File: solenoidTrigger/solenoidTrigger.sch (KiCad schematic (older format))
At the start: 41 parts, among them J8 CONN_02X03, P1 OSTTC03, P2 OSTTC02, P3 OSTTC08, P4 OSTTC03, P5 OSTTC03, Q1 NMOS_CDS16, Q2 NMOS_CDS16, Q3 NMOS_CDS16, Q4 NMOS_CDS16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

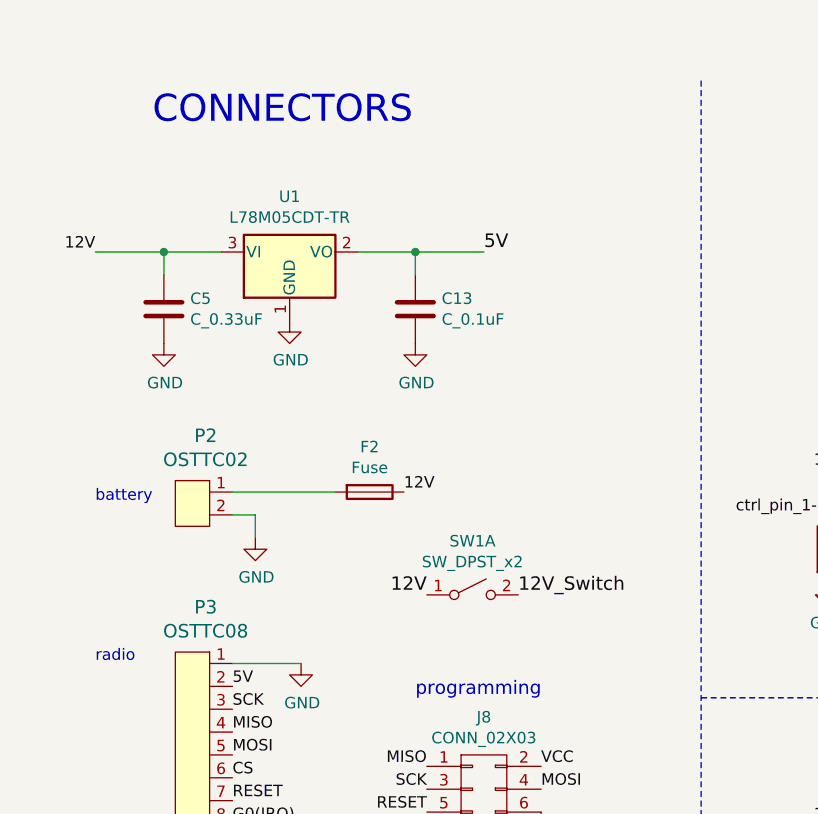
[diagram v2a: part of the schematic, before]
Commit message: Created part for fuse reciprocal, deleted most traces, laying out board again to improve organization and performance
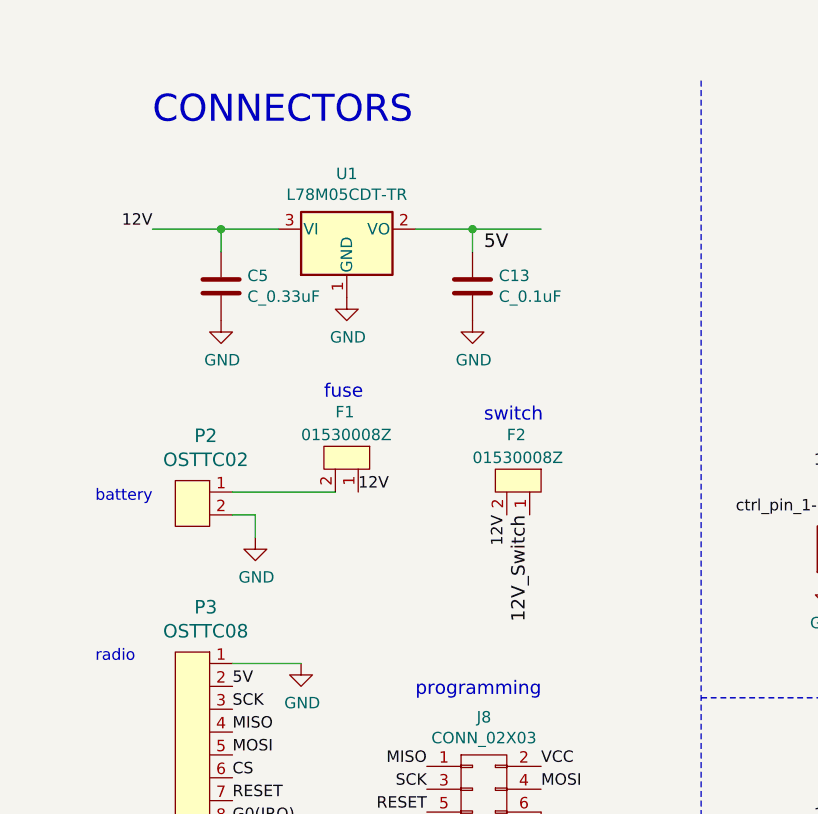
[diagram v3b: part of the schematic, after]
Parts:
- removed F2: Fuse, symbol Device:Fuse
- removed SW1: SW_DPST_x2, symbol Switch:SW_DPST_x2
- added F1, F2: 01530008Z, footprints:01530008Z, symbol Rocketry:01530008Z
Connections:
- net 12V: now also F1.1, F2.2
- net 12V_Switch: now also F2.1
- net VCC: no longer C13.1, U1.2 (VO)
- net at P2.1: now also F1.2
- new net: C13.1, U1.2 (VO)
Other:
- note added: "fuse"
- note added: "switch\n"
- moved on the sheet: C13, C5, U1
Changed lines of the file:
@@
 Text Label 2750 9750 0    50   ~ 0
 12V_Solenoid3
-Text Label 2300 7350 0    50   ~ 0
-12V
 Text Notes 950  7400 0    50   ~ 0
 battery
@@
 Wire Wire Line
 	1650 7450 1650 7550
-$Comp
-L Device:Fuse F2
-U 1 1 5DA01504
-P 2150 7350
-F 0 "F2" V 1953 7350 50  0000 C CNN
-F 1 "Fuse" V 2044 7350 50  0000 C CNN
-F 2 "" V 2080 7350 50  0001 C CNN
-F 3 "~" H 2150 7350 50  0001 C CNN
-	1    2150 7350
-	0    1    1    0
-$EndComp
 Text Notes 2350 8250 0    59   ~ 0
 programming
@@
 L power:GND #PWR0131
 U 1 1 5DDAC02E
-P 2350 6700
-F 0 "#PWR0131" H 2350 6450 50  0001 C CNN
-F 1 "GND" H 2355 6527 50  0000 C CNN
-F 2 "" H 2350 6700 50  0001 C CNN
-F 3 "" H 2350 6700 50  0001 C CNN
-	1    2350 6700
+P 2600 6600
+F 0 "#PWR0131" H 2600 6350 50  0001 C CNN
+F 1 "GND" H 2605 6427 50  0000 C CNN
+F 2 "" H 2600 6600 50  0001 C CNN
+F 3 "" H 2600 6600 50  0001 C CNN
+	1    2600 6600
 	1    0    0    -1
 $EndComp
@@
 L Rocketry:C_0.1uF C13
 U 1 1 5DDAB0AE
-P 2350 6550
-F 0 "C13" H 2465 6596 50  0000 L CNN
-F 1 "C_0.1uF" H 2465 6505 50  0000 L CNN
-F 2 "footprints:C_0805_OEM" H 2388 6400 50  0001 C CNN
-F 3 "http://datasheets.avx.com/X7RDielectric.pdf" H 2375 6650 50  0001 C CNN
-F 4 "DK" H 2350 6550 60  0001 C CNN "MFN"
-F 5 "478-3352-1-ND" H 2350 6550 60  0001 C CNN "MPN"
-F 6 "https://www.digikey.com/products/en?keywords=478-3352-1-ND" H 2775 7050 60  0001 C CNN "PurchasingLink"
-	1    2350 6550
+P 2600 6450
+F 0 "C13" H 2715 6496 50  0000 L CNN
+F 1 "C_0.1uF" H 2715 6405 50  0000 L CNN
+F 2 "footprints:C_0805_OEM" H 2638 6300 50  0001 C CNN
+F 3 "http://datasheets.avx.com/X7RDielectric.pdf" H 2625 6550 50  0001 C CNN
+F 4 "DK" H 2600 6450 60  0001 C CNN "MFN"
+F 5 "478-3352-1-ND" H 2600 6450 60  0001 C CNN "MPN"
+F 6 "https://www.digikey.com/products/en?keywords=478-3352-1-ND" H 3025 6950 60  0001 C CNN "PurchasingLink"
+	1    2600 6450
 	1    0    0    -1
 $EndComp
 Wire Wire Line
-	2350 6300 2650 6300
-Connection ~ 2350 6300
+	2600 6200 2900 6200
+Connection ~ 2600 6200
 Wire Wire Line
-	2350 6300 2350 6400
+	2600 6200 2600 6300
 Wire Wire Line
-	2100 6300 2350 6300
+	2350 6200 2600 6200
 Text Label 2650 6300 0    59   ~ 0
 5V
@@
 L power:GND #PWR0124
 U 1 1 5DD00003
-P 1250 6700
-F 0 "#PWR0124" H 1250 6450 50  0001 C CNN
-F 1 "GND" H 1255 6527 50  0000 C CNN
-F 2 "" H 1250 6700 50  0001 C CNN
-F 3 "" H 1250 6700 50  0001 C CNN
-	1    1250 6700
+P 1500 6600
+F 0 "#PWR0124" H 1500 6350 50  0001 C CNN
+F 1 "GND" H 1505 6427 50  0000 C CNN
+F 2 "" H 1500 6600 50  0001 C CNN
+F 3 "" H 1500 6600 50  0001 C CNN
+	1    1500 6600
 	1    0    0    -1
 $EndComp
 Wire Wire Line
-	1250 6300 1500 6300
-Connection ~ 1250 6300
+	1500 6200 1750 6200
+Connection ~ 1500 6200
 Wire Wire Line
-	1250 6300 1250 6400
+	1500 6200 1500 6300
 Wire Wire Line
-	950  6300 1250 6300
+	1200 6200 1500 6200
 $Comp
 L Rocketry:C_0.33uF C5
 U 1 1 5DEDBC87
-P 1250 6550
-F 0 "C5" H 1135 6504 50  0000 R CNN
-F 1 "C_0.33uF" H 1135 6595 50  0000 R CNN
-F 2 "footprints:C_0805_OEM" H 1288 6400 50  0001 C CNN
-F 3 "http://datasheets.avx.com/X7RDielectric.pdf" H 1275 6650 50  0001 C CNN
-F 4 "DK" H 1250 6550 60  0001 C CNN "MFN"
-F 5 "478-5273-1-ND" H 1250 6550 60  0001 C CNN "MPN"
-F 6 "https://www.digikey.com/products/en/capacitors/ceramic-capacitors/60?k=cap&k=&pkeyword=cap&pv7=2&pv7=274&pv7=250&pv7=17&pv7=6&pv1989=0&pv2049=u0.33%C2%B5F&pv3=2&pv14=9&pv16=6&sf=1&FV=ffe0003c&quantity=&ColumnSort=0&page=1&stock=1&datasheet=1&pageSize=25" H 1675 7050 60  0001 C CNN "PurchasingLink"
-	1    1250 6550
+P 1500 6450
+F 0 "C5" H 1385 6404 50  0000 R CNN
+F 1 "C_0.33uF" H 1385 6495 50  0000 R CNN
+F 2 "footprints:C_0805_OEM" H 1538 6300 50  0001 C CNN
+F 3 "http://datasheets.avx.com/X7RDielectric.pdf" H 1525 6550 50  0001 C CNN
+F 4 "DK" H 1500 6450 60  0001 C CNN "MFN"
+F 5 "478-5273-1-ND" H 1500 6450 60  0001 C CNN "MPN"
+F 6 "https://www.digikey.com/products/en/capacitors/ceramic-capacitors/60?k=cap&k=&pkeyword=cap&pv7=2&pv7=274&pv7=250&pv7=17&pv7=6&pv1989=0&pv2049=u0.33%C2%B5F&pv3=2&pv14=9&pv16=6&sf=1&FV=ffe0003c&quantity=&ColumnSort=0&page=1&stock=1&datasheet=1&pageSize=25" H 1925 6950 60  0001 C CNN "PurchasingLink"
+	1    1500 6450
 	-1   0    0    1
 $EndComp
@@
 L Regulator_Linear:AMS1117-5.0 U1
 U 1 1 5DDA38F2
-P 1800 6300
-F 0 "U1" H 1800 6542 50  0000 C CNN
-F 1 "L78M05CDT-TR " H 1800 6451 50  0000 C CNN
-F 2 "footprints:L78M05CDT-TR" H 1800 6500 50  0001 C CNN
-F 3 "www.st.com/content/ccc/resource/technical/document/datasheet/d7/5f/dc/5c/d5/b6/48/7c/CD00000447.pdf/files/CD00000447.pdf/jcr:content/translations/en.CD00000447.pdf" H 1900 6050 50  0001 C CNN
-	1    1800 6300
+P 2050 6200
+F 0 "U1" H 2050 6442 50  0000 C CNN
+F 1 "L78M05CDT-TR " H 2050 6351 50  0000 C CNN
+F 2 "footprints:L78M05CDT-TR" H 2050 6400 50  0001 C CNN
+F 3 "www.st.com/content/ccc/resource/technical/document/datasheet/d7/5f/dc/5c/d5/b6/48/7c/CD00000447.pdf/files/CD00000447.pdf/jcr:content/translations/en.CD00000447.pdf" H 2150 5950 50  0001 C CNN
+	1    2050 6200
 	1    0    0    -1
 $EndComp
@@
 L power:GND #PWR0118
 U 1 1 5DEE7B7E
-P 1800 6600
-F 0 "#PWR0118" H 1800 6350 50  0001 C CNN
-F 1 "GND" H 1805 6427 50  0000 C CNN
-F 2 "" H 1800 6600 50  0001 C CNN
-F 3 "" H 1800 6600 50  0001 C CNN
-	1    1800 6600
-	1    0    0    -1
-$EndComp
-Text Label 950  6300 2    50   ~ 0
+P 2050 6500
+F 0 "#PWR0118" H 2050 6250 50  0001 C CNN
+F 1 "GND" H 2055 6327 50  0000 C CNN
+F 2 "" H 2050 6500 50  0001 C CNN
+F 3 "" H 2050 6500 50  0001 C CNN
+	1    2050 6500
+	1    0    0    -1
+$EndComp
+Text Label 1200 6200 2    50   ~ 0
 12V
 Text Notes 1200 5750 0    118  ~ 0
@@
 Wire Notes Line
 	3600 9700 7950 9700
-$Comp
-L Switch:SW_DPST_x2 SW1
-U 1 1 5DE0F544
-P 2600 7800
-F 0 "SW1" H 2600 8035 50  0000 C CNN
-F 1 "SW_DPST_x2" H 2600 7944 50  0000 C CNN
-F 2 "" H 2600 7800 50  0001 C CNN
-F 3 "~" H 2600 7800 50  0001 C CNN
-	1    2600 7800
-	1    0    0    -1
-$EndComp
-Text Label 2400 7800 2    59   ~ 0
-12V
-Text Label 2800 7800 0    59   ~ 0
-12V_Switch
 Wire Notes Line
 	7950 6650 7950 11100
@@
 	1    0    0    -1
 $EndComp
+Text Label 2100 7350 0    50   ~ 0
+12V
+$Comp
+L Rocketry:01530008Z F1
+U 1 1 5DF76EC6
+P 2300 7250
+F 0 "F1" V 2050 6950 50  0000 L CNN
+F 1 "01530008Z" V 2150 6800 50  0000 L CNN
+F 2 "footprints:01530008Z" H 2250 7050 50  0001 C CNN
+F 3 "https://www.littelfuse.com/~/media/commercial-vehicle/datasheets/automotive-fuse-holders/mini/littelfuse_fuse-holders-mini-153-pc-datasheet.pdf" H 2250 7050 50  0001 C CNN
+F 4 "01530008Z" H 2400 7250 50  0001 C CNN "MPN"
+F 5 "F065-ND" H 2400 7250 50  0001 C CNN "DPN"
+F 6 "https://www.digikey.com/product-detail/en/littelfuse-inc/01530008Z/F065-ND/183334" H 2400 7250 50  0001 C CNN "Purchasing Link"
+F 7 "This is just a fuse reciprocal, the fuse it will hold is 0297010.WXNV (https://www.digikey.com/product-detail/en/littelfuse-inc/0297010.WXNV/F991-ND/146591)" H 2400 7250 50  0001 C CNN "Notes"
+	1    2300 7250
+	0    1    1    0
+$EndComp
+Text Label 2750 7450 3    50   ~ 0
+12V
+$Comp
+L Rocketry:01530008Z F2
+U 1 1 5DF8F17C
+P 3050 7350
+F 0 "F2" V 2800 7050 50  0000 L CNN
+F 1 "01530008Z" V 2900 6900 50  0000 L CNN
+F 2 "footprints:01530008Z" H 3000 7150 50  0001 C CNN
+F 3 "https://www.littelfuse.com/~/media/commercial-vehicle/datasheets/automotive-fuse-holders/mini/littelfuse_fuse-holders-mini-153-pc-datasheet.pdf" H 3000 7150 50  0001 C CNN
+F 4 "01530008Z" H 3150 7350 50  0001 C CNN "MPN"
+F 5 "F065-ND" H 3150 7350 50  0001 C CNN "DPN"
+F 6 "https://www.digikey.com/product-detail/en/littelfuse-inc/01530008Z/F065-ND/183334" H 3150 7350 50  0001 C CNN "Purchasing Link"
+F 7 "This is just a fuse reciprocal, the fuse it will hold is 0297010.WXNV (https://www.digikey.com/product-detail/en/littelfuse-inc/0297010.WXNV/F991-ND/146591)" H 3150 7350 50  0001 C CNN "Notes"
+	1    3050 7350
+	0    1    1    0
+$EndComp
+Text Label 2850 7450 3    59   ~ 0
+12V_Switch
+Text Notes 2650 7050 0    59   ~ 0
+switch\n
+Text Notes 1950 6950 0    59   ~ 0
+fuse
 $EndSCHEMATC

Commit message: moved around oscillator
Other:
- note added: "- some pins and their purposes in the schematic don't match the pinout diagram\n- in the layout editor, some of the pins don't match the schematic: (ground pins at 3, 5, 21 and VCC at 4,6)"
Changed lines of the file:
@@
 Text Notes 1950 6950 0    59   ~ 0
 fuse
+Text Notes 5100 5000 0    59   ~ 0
+- some pins and their purposes in the schematic don't match the pinout diagram\n- in the layout editor, some of the pins don't match the schematic: (ground pins at 3, 5, 21 and VCC at 4,6)
 $EndSCHEMATC

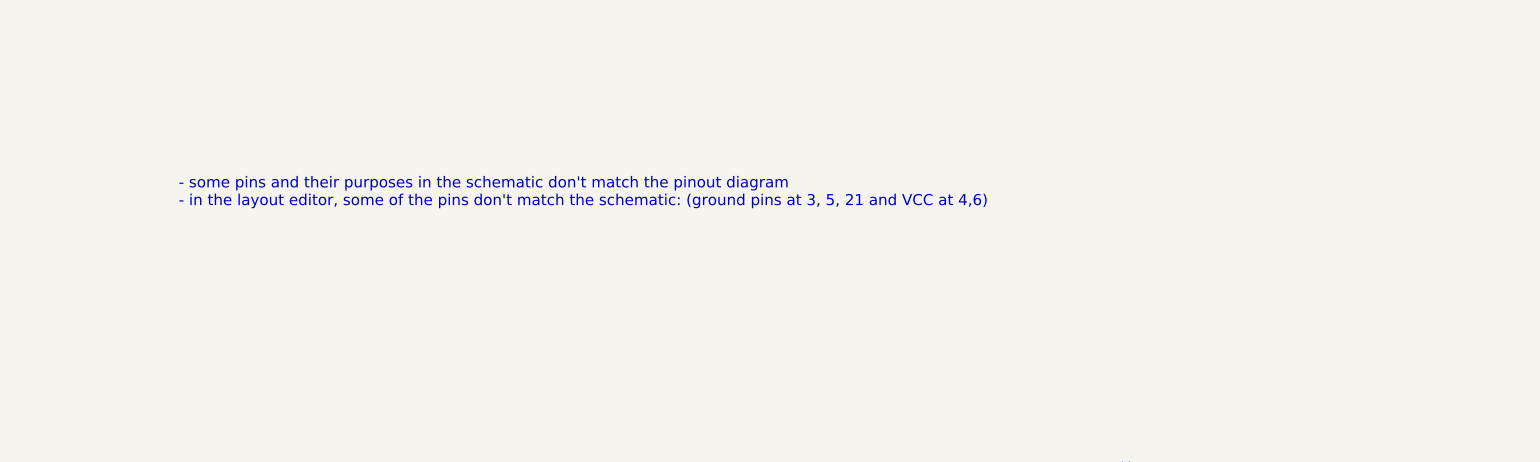
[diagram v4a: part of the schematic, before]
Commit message: moved purple to left side of atmega
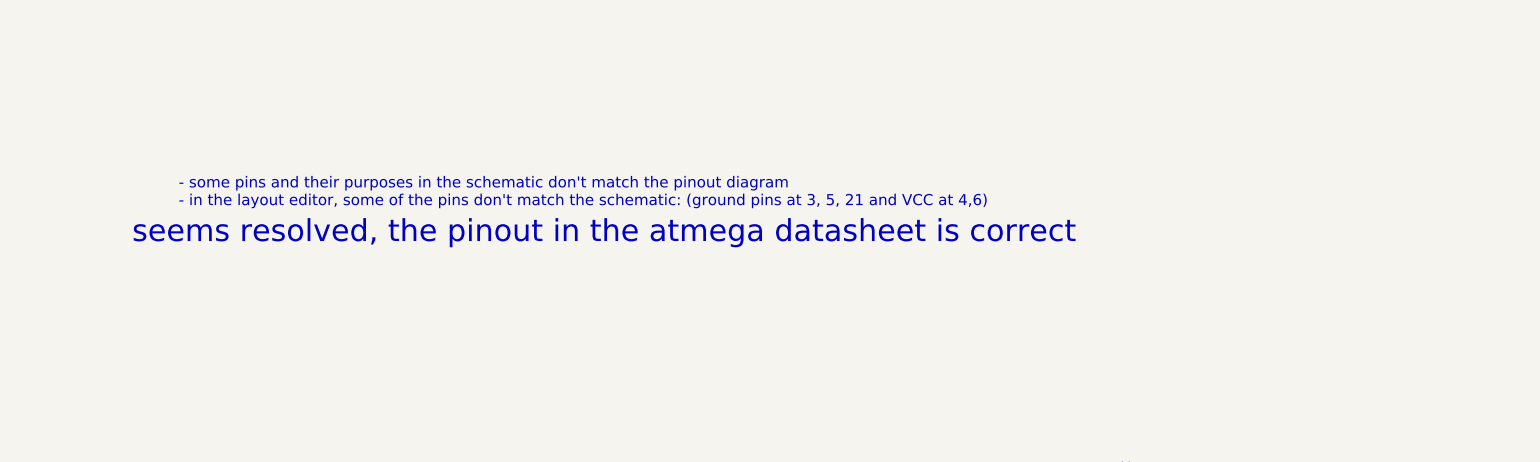
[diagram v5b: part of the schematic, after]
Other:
- note added: "seems resolved, the pinout in the atmega datasheet is correct\n"
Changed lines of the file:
@@
 Text Notes 5100 5000 0    59   ~ 0
 - some pins and their purposes in the schematic don't match the pinout diagram\n- in the layout editor, some of the pins don't match the schematic: (ground pins at 3, 5, 21 and VCC at 4,6)
+Text Notes 4850 5200 0    118  ~ 0
+seems resolved, the pinout in the atmega datasheet is correct\n
 $EndSCHEMATC

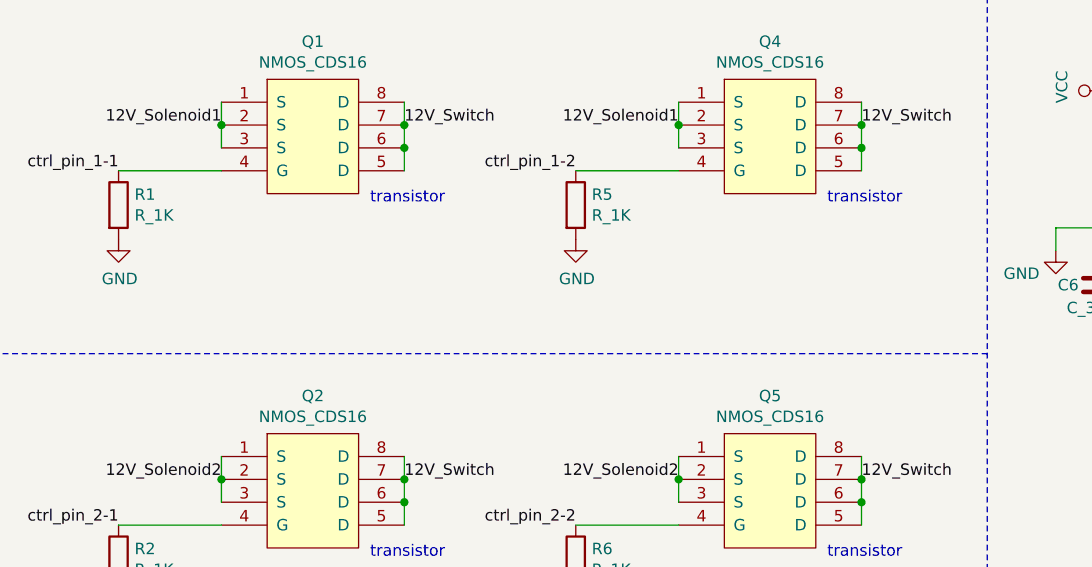
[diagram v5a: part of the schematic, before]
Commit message: added flyback diode
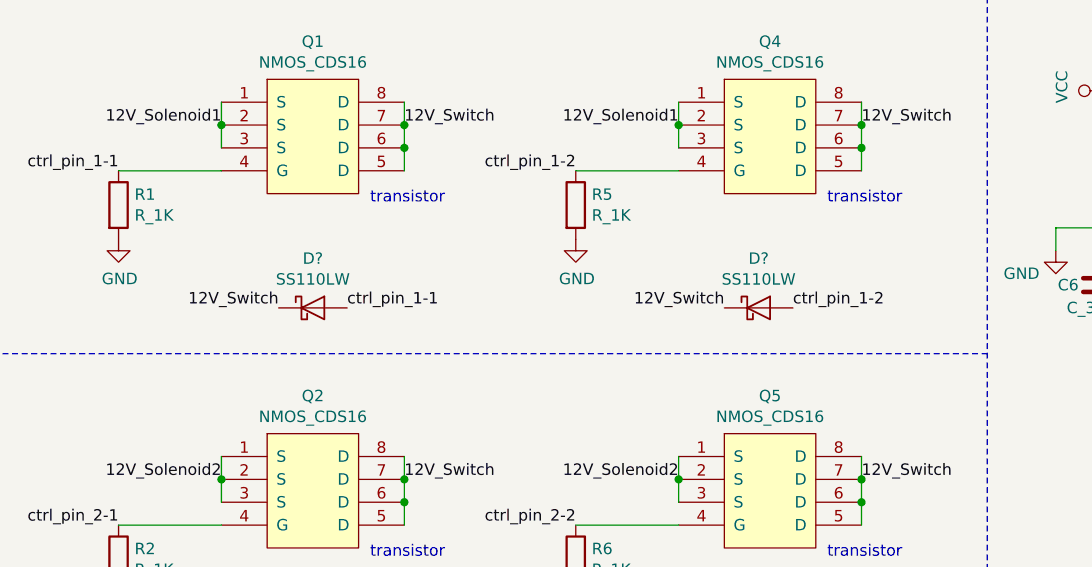
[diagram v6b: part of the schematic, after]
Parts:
- added D? (x2): SS110LW, footprints:D_SOD-123W_OEM, symbol Rocketry:SS110LW
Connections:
- net 12V_Switch: now also D?.1 (K), D?.1 (K)
- net ctrl_pin_1-1: now also D?.2 (A)
- net ctrl_pin_1-2: now also D?.2 (A)
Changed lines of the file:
@@
 Text Notes 4850 5200 0    118  ~ 0
 seems resolved, the pinout in the atmega datasheet is correct\n
+$Comp
+L Rocketry:SS110LW D?
+U 1 1 5E107C0A
+P 5000 8050
+F 0 "D?" H 5000 8266 50  0000 C CNN
+F 1 "SS110LW" H 5000 8175 50  0000 C CNN
+F 2 "footprints:D_SOD-123W_OEM" H 4900 8050 50  0001 C CNN
+F 3 "http://www.taiwansemi.com/products/datasheet/SS14LW%20SERIES_A1511.pdf" H 5000 8150 50  0001 C CNN
+F 4 "DK" H 5200 8350 60  0001 C CNN "MFN"
+F 5 "SS110LWRVGCT-ND" H 5100 8250 60  0001 C CNN "MPN"
+F 6 "https://www.digikey.com/product-detail/en/taiwan-semiconductor-corporation/SS110LW-RVG/SS110LWRVGCT-ND/7359346" H 5300 8450 60  0001 C CNN "PurchasingLink"
+	1    5000 8050
+	1    0    0    -1
+$EndComp
+Text Label 5150 8050 0    50   ~ 0
+ctrl_pin_1-1
+Text Label 4850 8050 2    50   ~ 0
+12V_Switch
+$Comp
+L Rocketry:SS110LW D?
+U 1 1 5E14DE1F
+P 6950 8050
+F 0 "D?" H 6950 8266 50  0000 C CNN
+F 1 "SS110LW" H 6950 8175 50  0000 C CNN
+F 2 "footprints:D_SOD-123W_OEM" H 6850 8050 50  0001 C CNN
+F 3 "http://www.taiwansemi.com/products/datasheet/SS14LW%20SERIES_A1511.pdf" H 6950 8150 50  0001 C CNN
+F 4 "DK" H 7150 8350 60  0001 C CNN "MFN"
+F 5 "SS110LWRVGCT-ND" H 7050 8250 60  0001 C CNN "MPN"
+F 6 "https://www.digikey.com/product-detail/en/taiwan-semiconductor-corporation/SS110LW-RVG/SS110LWRVGCT-ND/7359346" H 7250 8450 60  0001 C CNN "PurchasingLink"
+	1    6950 8050
+	1    0    0    -1
+$EndComp
+Text Label 7100 8050 0    50   ~ 0
+ctrl_pin_1-2
+Text Label 6800 8050 2    50   ~ 0
+12V_Switch
 $EndSCHEMATC

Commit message: I think I have finished the final schematic, added flybacks and second fuse
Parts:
- removed D?: SS110LW, footprints:D_SOD-123W_OEM, symbol Rocketry:SS110LW
- added D10, D11, D2, D7, D9: SS110LW, footprints:D_SOD-123W_OEM, symbol Rocketry:SS110LW
- added F3: 01530008Z, footprints:01530008Z, symbol Rocketry:01530008Z
- gave numbers to parts that had none: 1
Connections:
- net 12V_Solenoid1: now also D8.2 (A), D9.2 (A)
- net 12V_Solenoid2: now also D10.2 (A), D2.2 (A)
- net 12V_Solenoid3: now also D11.2 (A), D7.2 (A)
- net 12V_Switch: now also D10.1 (K), D11.1 (K), D2.1 (K), D7.1 (K), D9.1 (K)
- net VCC: now also C13.1, U1.2 (VO)
- net ctrl_pin_1-1: no longer D8.2 (A)
- net Source(12V): now reaches F1.2, P2.1
- net Source(12V): now also R10.1, F3.2
- net 12V renamed 12V_Low
- net 12V_Low: no longer F2.2, R10.1
- new net 12V_High: F2.2, F3.1
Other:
- note added: "high-power fuse"
- note added: "linear\nregulator\n"
- note added: "low-power fuse"
- note removed: "fuse"
- moved on the sheet: C13, C5, F1, F2, J8, P1, P2, P3, P4, P5, U1
